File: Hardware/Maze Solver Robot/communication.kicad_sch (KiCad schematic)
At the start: 6 parts

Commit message: Add final changes
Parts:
- added R? (x2): 4.7k, symbol Device:R_US
- added SW? (x2): SW_Push, symbol Switch:SW_Push
- D? (x3): value LED -> RED_LED
- R? (x3): value R_US -> 33
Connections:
- net 3.3V: now also R?.1, R?.1; no longer D?.2 (A), D?.2 (A), D?.2 (A)
- new net: R?.2, SW?.2 (x2)
- new net B1: SW?.1
- new net B2: SW?.1
- new net LED1: D?.2 (A)
- new net LED2: D?.2 (A)
- new net LED3: D?.2 (A)
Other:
- moved on the sheet: D?, R?

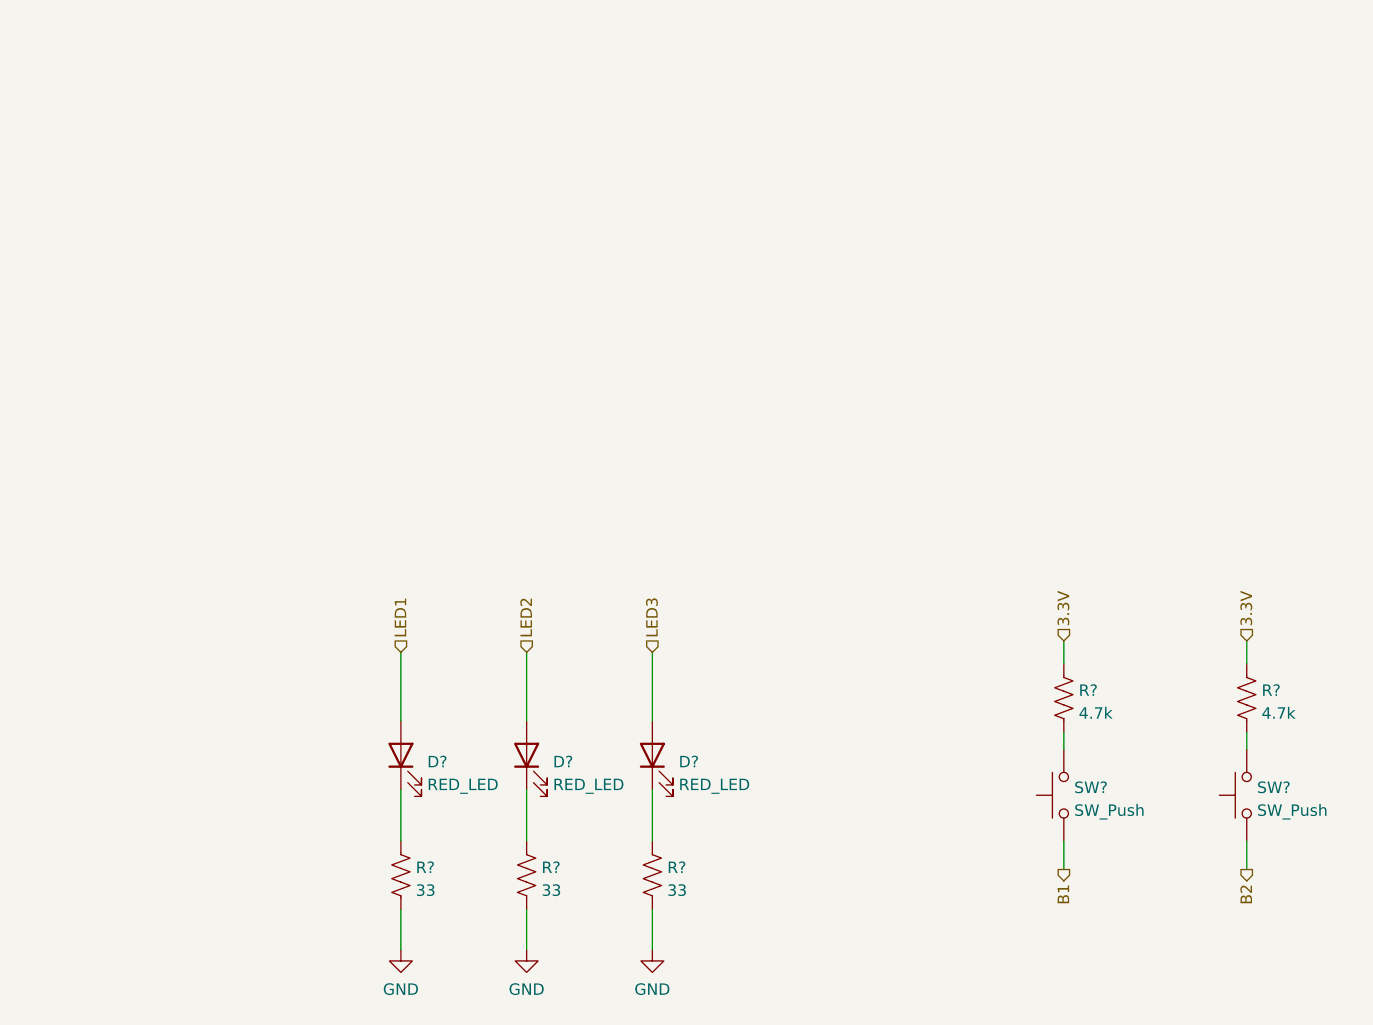
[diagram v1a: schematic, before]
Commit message: Add comments to schematics
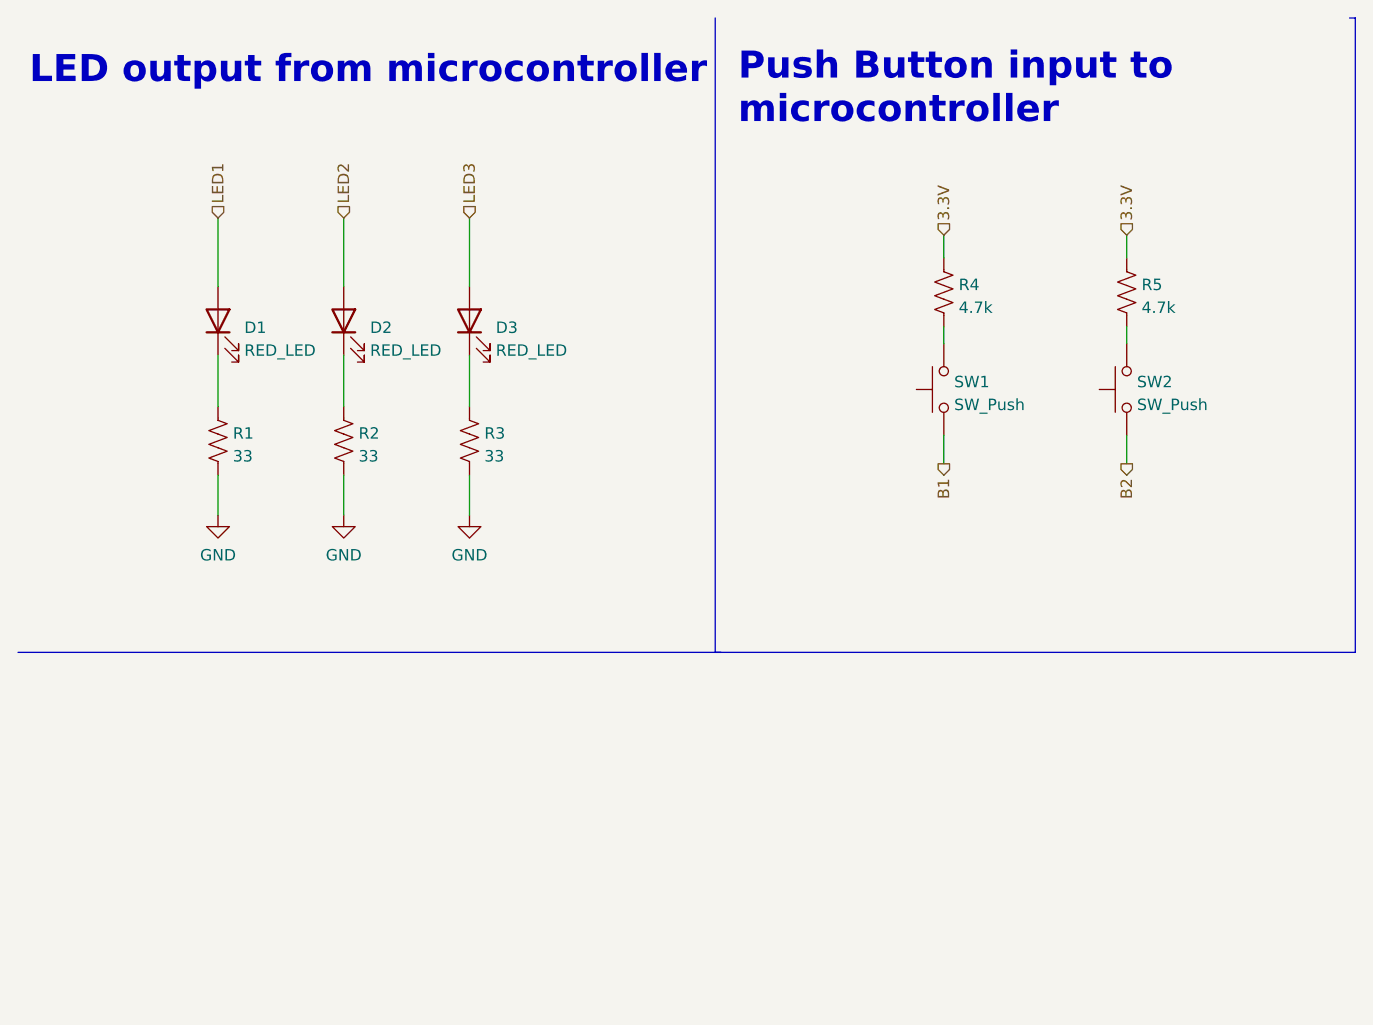
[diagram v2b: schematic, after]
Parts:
- gave numbers to parts that had none: 10
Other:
- note added: "LED output from microcontroller"
- note added: "Push Button input to microcontroller"
- moved on the sheet: D1, D2, D3, R1, R2, R3, R4, R5, SW1, SW2
